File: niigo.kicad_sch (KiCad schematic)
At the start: 7 parts, among them Q1 BC547, SW1 SW_Push

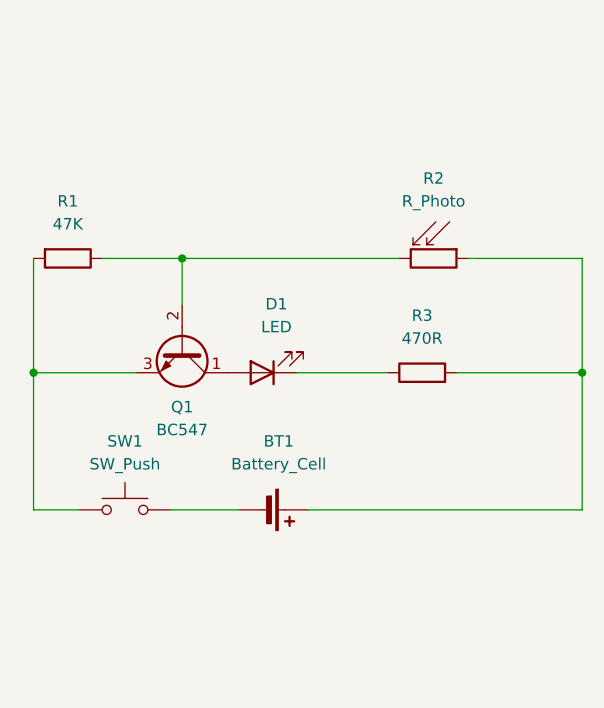
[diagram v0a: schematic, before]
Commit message: v2.0 (+ .gbr and .srl files!)
v2.0 adds a vibrating motor with the motor disc given in the set (and more resistors...) and the gerbel and drill files needed for submission have been uploaded!
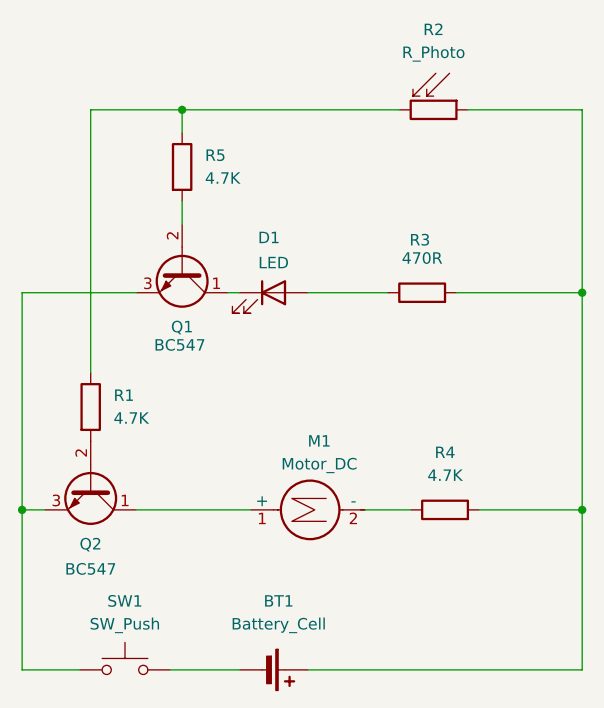
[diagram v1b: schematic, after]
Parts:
- added M1: Motor_DC, Connector_PinHeader_1.00mm:PinHeader_2x01_P1.00mm_Horizontal, symbol Motor:Motor_DC
- added Q2: BC547, Package_TO_SOT_THT:TO-92_Inline, symbol Transistor_BJT:BC547
- added R4, R5: 4.7K, Resistor_THT:R_Axial_DIN0207_L6.3mm_D2.5mm_P7.62mm_Horizontal, symbol Device:R
- R1: value 47K -> 4.7K; footprint Resistor_THT:R_Axial_DIN0411_L9.9mm_D3.6mm_P7.62mm_Vertical -> Resistor_THT:R_Axial_DIN0207_L6.3mm_D2.5mm_P7.62mm_Horizontal
- R3: footprint Resistor_THT:R_Axial_DIN0411_L9.9mm_D3.6mm_P7.62mm_Vertical -> Resistor_THT:R_Axial_DIN0207_L6.3mm_D2.5mm_P7.62mm_Horizontal
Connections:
- net at Q1.1 (C): now also D1.1 (K); no longer D1.2 (A)
- net at R1.1, R2.2: now also R5.1; no longer Q1.2 (B)
- net at Q1.3 (E), SW1.1: now also Q2.3 (E); no longer R1.2
- net at BT1.1 (+), R2.1, R3.2: now also R4.2
- net at R3.1: now also D1.2 (A); no longer D1.1 (K)
- new net: Q1.2 (B), R5.2
- new net: M1.2 (-), R4.1
- new net: Q2.2 (B), R1.2
- new net: M1.1 (+), Q2.1 (C)
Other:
- moved on the sheet: BT1, D1, Q1, R2, R3, SW1
